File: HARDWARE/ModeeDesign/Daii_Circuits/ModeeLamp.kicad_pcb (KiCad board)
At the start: 2 copper layers, 26 x 49 mm, 12 parts, among them J1 AC, J2 PW_SUPP_OUT, J3 DS18B20, Q1 2N2222, Q2 IRLZ44N, U2 MOC3023M

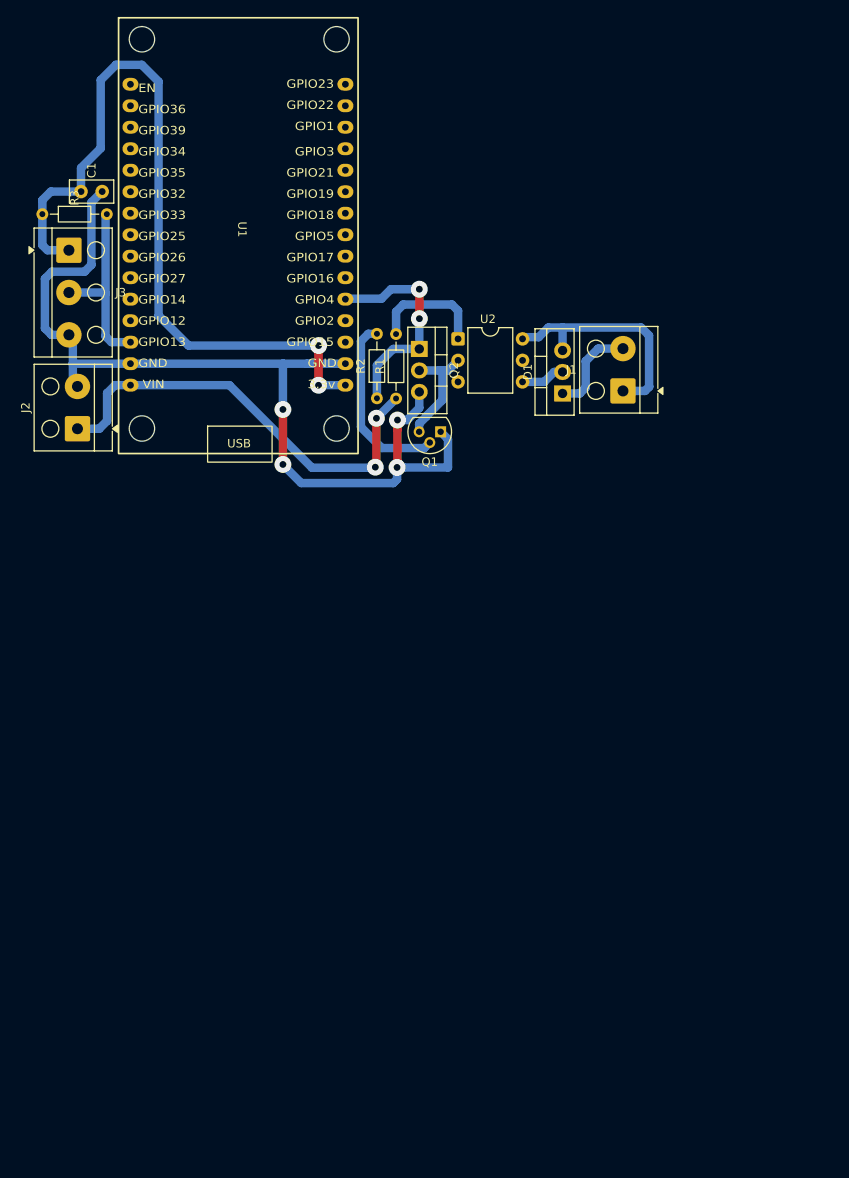
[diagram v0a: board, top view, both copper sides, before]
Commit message: Fixing PCB review points and add interactive BOM
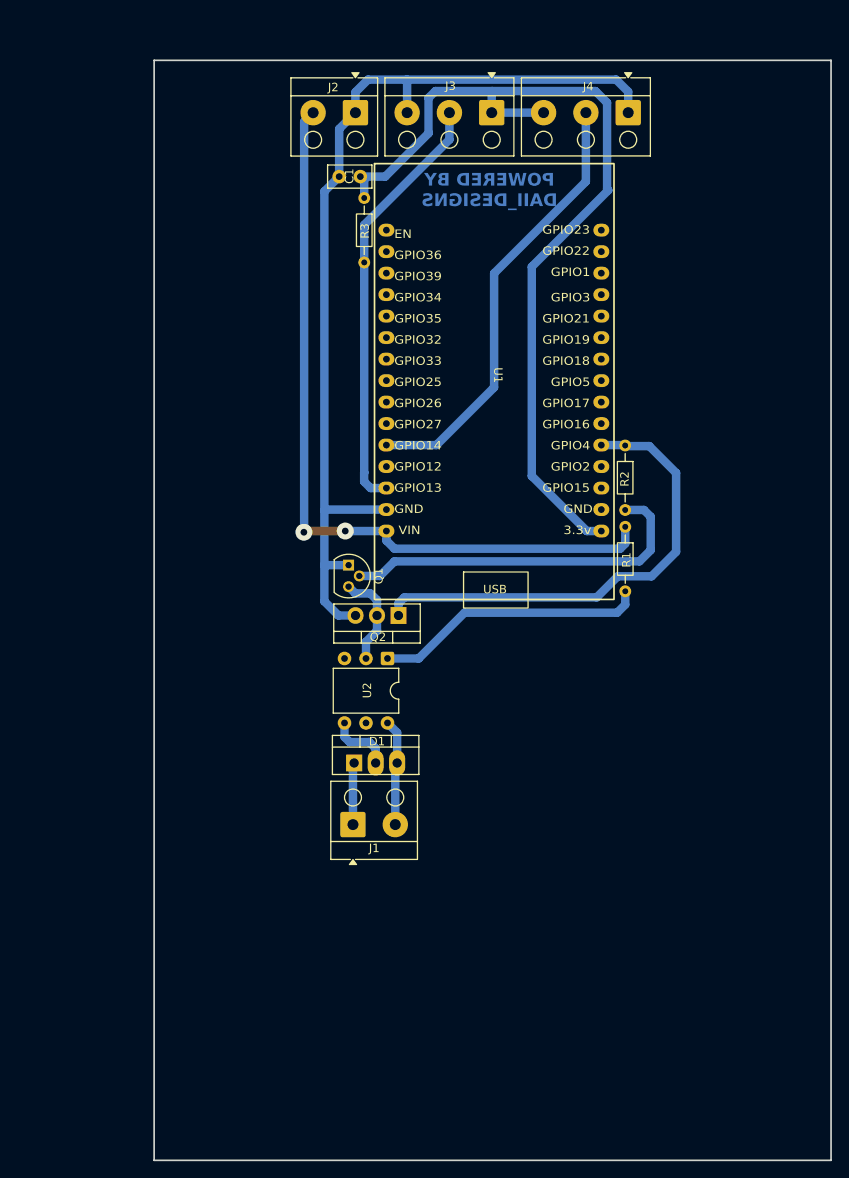
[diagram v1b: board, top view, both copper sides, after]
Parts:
- added J4: TTP223, TerminalBlock_Altech:Altech_AK100_1x03_P5.00mm, F.Cu at (161.9, 59.8)
- R1: value 10K -> 470
- moved J1 60.4 mm to (129.4, 143.9), turned to 0 degrees
- moved J3 52.5 mm to (145.8, 59.8), turned to 180 degrees
- moved D1 50.1 mm to (129.5, 136.7), turned to 0 degrees
- moved J2 49.7 mm to (129.7, 59.8), turned to 180 degrees
- moved U2 38.7 mm to (133.4, 124.3), turned to -90 degrees
- moved R3 38.1 mm to (130.7, 69.9), turned to -90 degrees
- moved U1 34.8 mm to (145.2, 92.2)
- moved C1 33.1 mm to (130.2, 67.4), turned to 180 degrees
- moved Q2 31.6 mm to (134.8, 119.2), turned to 180 degrees
- moved R1 31.0 mm to (161.6, 108.8), turned to -90 degrees
- moved R2 29.9 mm to (161.5, 99.2), turned to -90 degrees
- moved Q1 19.2 mm to (128.8, 113.3), turned to -90 degrees
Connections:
- C1 pad 2: GND -> /GND
- J1 pad 1: Net-(D1-A2) -> Net-(D1-A1)
- J1 pad 2: Net-(D1-A1) -> Net-(D1-A2)
- J2 pad 1: VCC -> /GND
- J2 pad 2: GND -> /5V
- J3 pad 3: GND -> /GND
- Q1 pad 1: GND -> /GND
- Q2 pad 3: GND -> /GND
- R1 pad 1: VCC -> /5V
- U1 pad 1: VCC -> /5V
- U1 pad 17: GND -> unconnected-(U1-GND-Pad17)
- U1 pad 2: GND -> /GND
- U1 pad 5: unconnected-(U1-GPIO14-Pad5) -> /TTP_TOUCH
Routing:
- net /GND: track 0.00 -> 116.1 mm
- net GND: track 112.3 -> 0.00 mm, vias 4 -> 0
- net /5V: track 0.00 -> 91.8 mm, vias 0 -> 2
- net /TTP_TOUCH: track 0.00 -> 52.5 mm
- net VCC: track 52.5 -> 0.00 mm, vias 2 -> 0
- net /LED_PWM: track 26.0 -> 56.3 mm, vias 2 -> 0
- net /TEMP: track 22.1 -> 50.7 mm
- net Net-(Q1-B): track 21.8 -> 43.0 mm
- net Net-(R1-Pad2): track 13.9 -> 32.3 mm
- net Net-(D1-A2): track 28.0 -> 12.6 mm
- net /3.3V: track 92.1 -> 106.6 mm, vias 2 -> 0
- net Net-(D1-A1): track 11.3 -> 7.34 mm
- net Net-(D1-G): track 5.21 -> 7.62 mm
- net Net-(Q1-C): track 13.5 -> 11.5 mm
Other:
- board size 26 x 49 mm -> 80 x 130 mm
- board text added: "POWERED BY DAII_DESIGNS"
